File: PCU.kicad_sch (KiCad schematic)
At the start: 12 parts, among them J11 Screw_Terminal_01x01, U4 EPC2152, Y1 AMDLA4020S-220MT

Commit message: Final addings
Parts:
- removed J11: Screw_Terminal_01x01, TerminalBlock_Phoenix:TerminalBlock_Phoenix_MKDS-1,5-2-5.08_1x02_P5.08mm_Horizontal, symbol Connector:Screw_Terminal_01x01
- added J11: Screw_Terminal_01x04, TerminalBlock_Phoenix:TerminalBlock_Phoenix_MKDS-1,5-4-5.08_1x04_P5.08mm_Horizontal, symbol Connector:Screw_Terminal_01x04
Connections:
- net V_in_12V: now also J11.1 (Pin_1)
- net V_out: now also J11.2 (Pin_2)
- net at C8.1, U4.1 (Vdd12F): now also J11.3 (Pin_3)
- new net GND: J11.4 (Pin_4)
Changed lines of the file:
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@@
+	)
+	(junction
+		(at 149.86 52.07)
+		(diameter 0)
+		(color 0 0 0 0)
 	)
 	(junction
@@
 	(wire
 		(pts
+			(xy 59.69 45.72) (xy 66.04 45.72)
+		)
+		(stroke
+			(width 0)
+			(type default)
+		)
+	)
+	(wire
+		(pts
 			(xy 187.96 87.63) (xy 177.8 87.63)
 		)
@@
 	(wire
 		(pts
+			(xy 66.04 45.72) (xy 66.04 52.07)
+		)
+		(stroke
+			(width 0)
+			(type default)
+		)
+	)
+	(wire
+		(pts
 			(xy 153.67 68.58) (xy 153.67 72.39)
 		)
@@
 	(wire
 		(pts
+			(xy 54.61 30.48) (xy 59.69 30.48)
+		)
+		(stroke
+			(width 0)
+			(type default)
+		)
+	)
+	(wire
+		(pts
+			(xy 54.61 27.94) (xy 189.23 27.94)
+		)
+		(stroke
+			(width 0)
+			(type default)
+		)
+	)
+	(wire
+		(pts
 			(xy 147.32 87.63) (xy 167.64 87.63)
 		)
@@
 	(wire
 		(pts
-			(xy 147.32 52.07) (xy 153.67 52.07)
+			(xy 59.69 30.48) (xy 59.69 45.72)
+		)
+		(stroke
+			(width 0)
+			(type default)
+		)
+	)
+	(wire
+		(pts
+			(xy 147.32 52.07) (xy 149.86 52.07)
 		)
 		(stroke
@@
 	(wire
 		(pts
+			(xy 54.61 20.32) (xy 54.61 22.86)
+		)
+		(stroke
+			(width 0)
+			(type default)
+		)
+	)
+	(wire
+		(pts
 			(xy 167.64 73.66) (xy 167.64 59.69)
 		)
@@
 	(wire
 		(pts
+			(xy 68.58 20.32) (xy 54.61 20.32)
+		)
+		(stroke
+			(width 0)
+			(type default)
+		)
+	)
+	(wire
+		(pts
+			(xy 149.86 52.07) (xy 153.67 52.07)
+		)
+		(stroke
+			(width 0)
+			(type default)
+		)
+	)
+	(wire
+		(pts
 			(xy 81.28 64.77) (xy 86.36 64.77)
 		)
@@
 	(wire
 		(pts
-			(xy 63.5 87.63) (xy 66.04 87.63)
+			(xy 149.86 52.07) (xy 149.86 25.4)
+		)
+		(stroke
+			(width 0)
+			(type default)
+		)
+	)
+	(wire
+		(pts
+			(xy 52.07 87.63) (xy 66.04 87.63)
 		)
 		(stroke
@@
 	(wire
 		(pts
+			(xy 149.86 25.4) (xy 54.61 25.4)
+		)
+		(stroke
+			(width 0)
+			(type default)
+		)
+	)
+	(wire
+		(pts
 			(xy 187.96 60.96) (xy 187.96 72.39)
+		)
+		(stroke
+			(width 0)
+			(type default)
+		)
+	)
+	(wire
+		(pts
+			(xy 189.23 27.94) (xy 189.23 60.96)
 		)
 		(stroke
@@
 	(hierarchical_label "GROUND"
 		(shape input)
-		(at 63.5 87.63 180)
+		(at 52.07 87.63 180)
 		(effects
 			(font
@@
 			)
 			(justify right)
+		)
+	)
+	(symbol
+		(lib_id "power:GND")
+		(at 68.58 20.32 0)
+		(unit 1)
+		(exclude_from_sim no)
+		(in_bom yes)
+		(on_board yes)
+		(dnp no)
+		(fields_autoplaced yes)
+		(property "Reference" "#PWR033"
+			(at 68.58 26.67 0)
+			(effects
+				(font
+					(size 1.27 1.27)
+				)
+				(hide yes)
+			)
+		)
+		(property "Value" "GND"
+			(at 68.58 25.4 0)
+			(effects
+				(font
+					(size 1.27 1.27)
+				)
+			)
+		)
+		(property "Footprint" ""
+			(at 68.58 20.32 0)
+			(effects
+				(font
+					(size 1.27 1.27)
+				)
+				(hide yes)
+			)
+		)
+		(property "Datasheet" ""
+			(at 68.58 20.32 0)
+			(effects
+				(font
+					(size 1.27 1.27)
+				)
+				(hide yes)
+			)
+		)
+		(property "Description" "Power symbol creates a global label with name \"GND\" , ground"
+			(at 68.58 20.32 0)
+			(effects
+				(font
+					(size 1.27 1.27)
+				)
+				(hide yes)
+			)
+		)
+		(pin "1"
+		)
+		(instances
+			(project "PULSE_ENG"
+				(path "/2de881bb-2e2a-47f9-96ed-b3393fa36b98/32fac869-3c72-4ec8-a514-1800b5db5371"
+					(reference "#PWR033")
+					(unit 1)
+				)
+			)
 		)
 	)
@@
 	)
 	(symbol
-		(lib_id "Connector:Screw_Terminal_01x01")
-		(at 194.31 60.96 0)
-		(unit 1)
-		(exclude_from_sim no)
-		(in_bom yes)
-		(on_board yes)
-		(dnp no)
-		(fields_autoplaced yes)
-		(property "Reference" "J11"
-			(at 196.85 59.6899 0)
-			(effects
-				(font
-					(size 1.27 1.27)
-				)
-				(justify left)
-			)
-		)
-		(property "Value" "Screw_Terminal_01x01"
-			(at 196.85 62.2299 0)
-			(effects
-				(font
-					(size 1.27 1.27)
-				)
-				(justify left)
-			)
-		)
-		(property "Footprint" "TerminalBlock_Phoenix:TerminalBlock_Phoenix_MKDS-1,5-2-5.08_1x02_P5.08mm_Horizontal"
-			(at 194.31 60.96 0)
-			(effects
-				(font
-					(size 1.27 1.27)
-				)
-				(hide yes)
-			)
-		)
-		(property "Datasheet" "~"
-			(at 194.31 60.96 0)
-			(effects
-				(font
-					(size 1.27 1.27)
-				)
-				(hide yes)
-			)
-		)
-		(property "Description" "Generic screw terminal, single row, 01x01, script generated (kicad-library-utils/schlib/autogen/connector/)"
-			(at 194.31 60.96 0)
-			(effects
-				(font
-					(size 1.27 1.27)
-				)
-				(hide yes)
-			)
-		)
-		(pin "1"
-		)
-		(instances
-			(project "PULSE_ENG"
-				(path "/2de881bb-2e2a-47f9-96ed-b3393fa36b98/32fac869-3c72-4ec8-a514-1800b5db5371"
-					(reference "J11")
-					(unit 1)
-				)
-			)
-		)
-	)
-	(symbol
 		(lib_id "SamacSys_Parts:EPC2152")
 		(at 91.44 90.17 0)
@@
 					(unit 1)
 				)
+			)
+		)
+	)
+	(symbol
+		(lib_id "Connector:Screw_Terminal_01x04")
+		(at 49.53 27.94 180)
+		(unit 1)
+		(exclude_from_sim no)
+		(in_bom yes)
+		(on_board yes)
+		(dnp no)
+		(fields_autoplaced yes)
+		(property "Reference" "J11"
+			(at 49.53 16.51 0)
+			(effects
+				(font
+					(size 1.27 1.27)
+				)
+			)
+		)
+		(property "Value" "Screw_Terminal_01x04"
+			(at 49.53 19.05 0)
+			(effects
+				(font
+					(size 1.27 1.27)
+				)
+			)
+		)
+		(property "Footprint" "TerminalBlock_Phoenix:TerminalBlock_Phoenix_MKDS-1,5-4-5.08_1x04_P5.08mm_Horizontal"
+			(at 49.53 27.94 0)
+			(effects
+				(font
+					(size 1.27 1.27)
+				)
+				(hide yes)
+			)
+		)
+		(property "Datasheet" "~"
+			(at 49.53 27.94 0)
+			(effects
+				(font
+					(size 1.27 1.27)
+				)
+				(hide yes)
+			)
+		)
+		(property "Description" "Generic screw terminal, single row, 01x04, script generated (kicad-library-utils/schlib/autogen/connector/)"
+			(at 49.53 27.94 0)
+			(effects
+				(font
+					(size 1.27 1.27)
+				)
+				(hide yes)
+			)
+		)
+		(pin "1"
+		)
+		(pin "2"
+		)
+		(pin "3"
+		)
+		(pin "4"
+		)
+		(instances
+			(project "PULSE_ENG"
+				(path "/2de881bb-2e2a-47f9-96ed-b3393fa36b98/32fac869-3c72-4ec8-a514-1800b5db5371"
+					(reference "J11")
+					(unit 1)
+				)

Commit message: Modofications asked and BOM
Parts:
- J11: Mouser Part Number (none) -> 651-1701144; Mouser link (none) -> https://www.mouser.ch/ProductDetail/Phoenix-Contact/1701144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
- L2: footprint Inductor_THT:L_Axial_L7.0mm_D3.3mm_P10.16mm_Horizontal_Fastron_MICC -> Inductor_SMD:L_0603_1608Metric
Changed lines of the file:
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@@
+			)
+		)
+		(property "Mouser Part Number" "651-1701144"
+			(at 49.53 27.94 0)
+			(effects
+				(font
+					(size 1.27 1.27)
+				)
+				(hide yes)
+			)
+		)
+		(property "Mouser link" "https://www.mouser.ch/ProductDetail/Phoenix-Contact/1701144?qs=2WS7V4AoKFp2%2F3%2FlSacg6Q%3D%3D"
+			(at 49.53 27.94 0)
+			(effects
+				(font
+					(size 1.27 1.27)
+				)
+				(hide yes)
 			)
 		)
@@
 			)
 		)
-		(property "Footprint" "Inductor_THT:L_Axial_L7.0mm_D3.3mm_P10.16mm_Horizontal_Fastron_MICC"
+		(property "Footprint" "Inductor_SMD:L_0603_1608Metric"
 			(at 161.29 72.39 0)
 			(effects

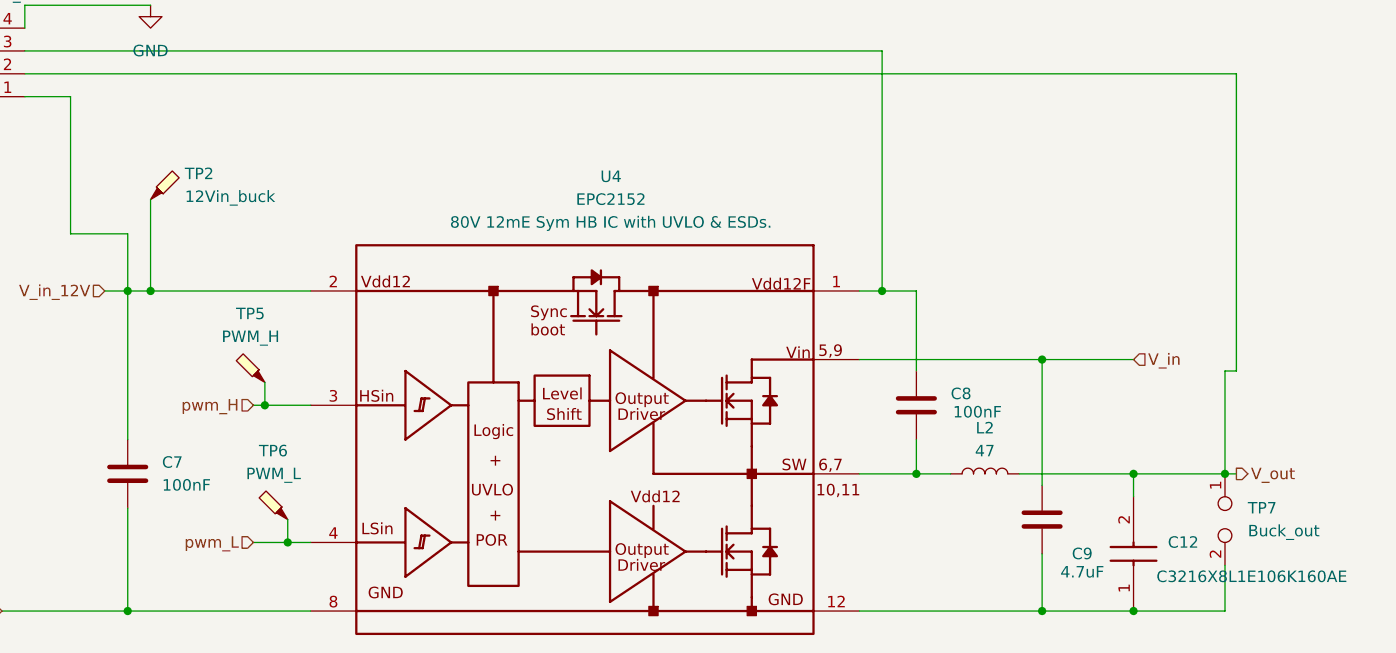
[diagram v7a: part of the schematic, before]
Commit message: changed mcu power suppl
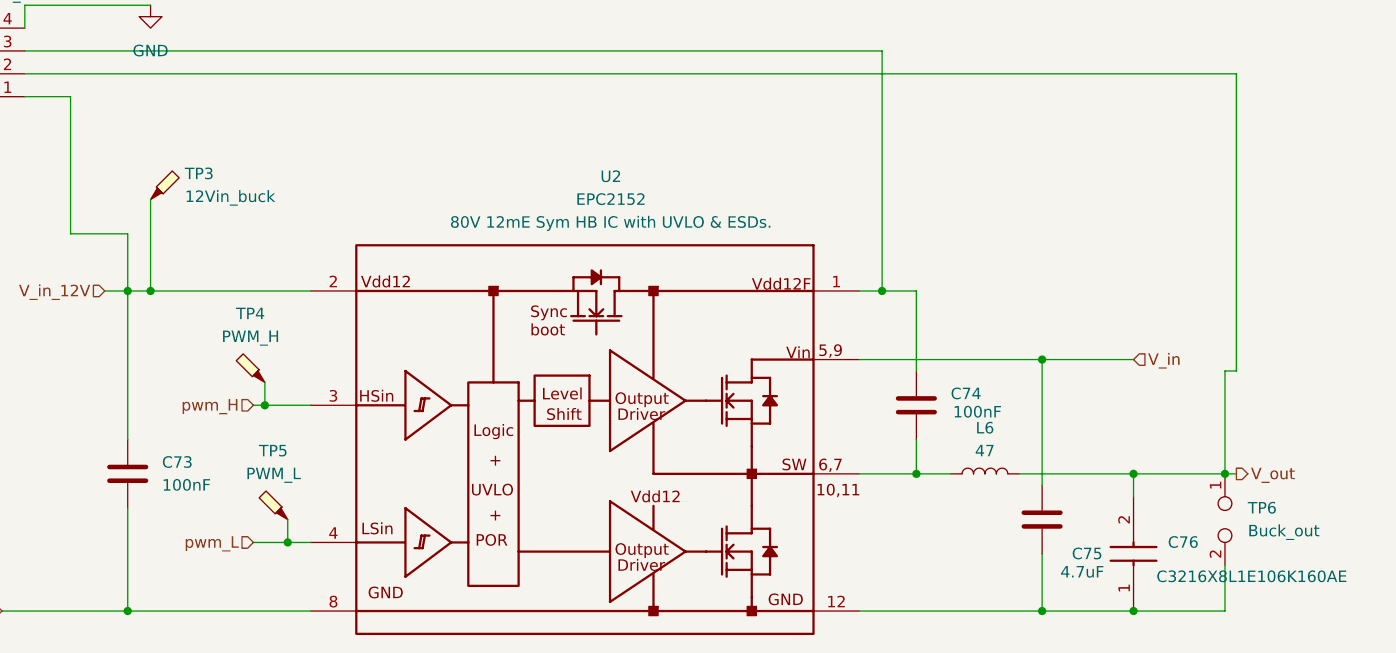
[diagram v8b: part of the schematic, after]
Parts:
- renumbered C7 to C73, C8 to C74, C9 to C75, C12 to C76, L2 to L6, TP2 to TP3, TP5 to TP4, TP6 to TP5, TP7 to TP6, U4 to U2
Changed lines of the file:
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@@
 		(dnp no)
 		(fields_autoplaced yes)
-		(property "Reference" "#PWR033"
+		(property "Reference" "#PWR048"
 			(at 68.58 26.67 0)
 			(effects
@@
 			(project "PULSE_ENG"
 				(path "/2de881bb-2e2a-47f9-96ed-b3393fa36b98/32fac869-3c72-4ec8-a514-1800b5db5371"
-					(reference "#PWR033")
+					(reference "#PWR048")
 					(unit 1)
 				)
@@
 		(dnp no)
 		(fields_autoplaced yes)
-		(property "Reference" "TP2"
+		(property "Reference" "TP3"
 			(at 72.39 39.0524 0)
 			(effects
@@
 			(project ""
 				(path "/2de881bb-2e2a-47f9-96ed-b3393fa36b98/32fac869-3c72-4ec8-a514-1800b5db5371"
-					(reference "TP2")
+					(reference "TP3")
 					(unit 1)
 				)
@@
 		(on_board yes)
 		(dnp no)
-		(property "Reference" "C12"
+		(property "Reference" "C76"
 			(at 181.61 80.0099 90)
 			(effects
@@
 			(project "PULSE_ENG"
 				(path "/2de881bb-2e2a-47f9-96ed-b3393fa36b98/32fac869-3c72-4ec8-a514-1800b5db5371"
-					(reference "C12")
+					(reference "C76")
 					(unit 1)
 				)
@@
 		(dnp no)
 		(fields_autoplaced yes)
-		(property "Reference" "TP6"
+		(property "Reference" "TP5"
 			(at 82.2325 69.85 90)
 			(effects
@@
 			(project "PULSE_ENG"
 				(path "/2de881bb-2e2a-47f9-96ed-b3393fa36b98/32fac869-3c72-4ec8-a514-1800b5db5371"
-					(reference "TP6")
+					(reference "TP5")
 					(unit 1)
 				)
@@
 		(on_board yes)
 		(dnp no)
-		(property "Reference" "C8"
+		(property "Reference" "C74"
 			(at 157.48 63.4999 0)
 			(effects
@@
 			(project "PULSE_ENG"
 				(path "/2de881bb-2e2a-47f9-96ed-b3393fa36b98/32fac869-3c72-4ec8-a514-1800b5db5371"
-					(reference "C8")
+					(reference "C74")
 					(unit 1)
 				)
@@
 		(dnp no)
 		(fields_autoplaced yes)
-		(property "Reference" "TP7"
+		(property "Reference" "TP6"
 			(at 190.5 76.1999 90)
 			(effects
@@
 			(project ""
 				(path "/2de881bb-2e2a-47f9-96ed-b3393fa36b98/32fac869-3c72-4ec8-a514-1800b5db5371"
-					(reference "TP7")
+					(reference "TP6")
 					(unit 1)
 				)
@@
 		(on_board yes)
 		(dnp no)
-		(property "Reference" "C9"
+		(property "Reference" "C75"
 			(at 170.942 81.28 0)
 			(effects
@@
 			(project "PULSE_ENG"
 				(path "/2de881bb-2e2a-47f9-96ed-b3393fa36b98/32fac869-3c72-4ec8-a514-1800b5db5371"
-					(reference "C9")
+					(reference "C75")
 					(unit 1)
 				)
@@
 		(dnp no)
 		(fields_autoplaced yes)
-		(property "Reference" "C7"
+		(property "Reference" "C73"
 			(at 69.85 71.1199 0)
 			(effects
@@
 			(project "PULSE_ENG"
 				(path "/2de881bb-2e2a-47f9-96ed-b3393fa36b98/32fac869-3c72-4ec8-a514-1800b5db5371"
-					(reference "C7")
+					(reference "C73")
 					(unit 1)
 				)
@@
 		(dnp no)
 		(fields_autoplaced yes)
-		(property "Reference" "U4"
+		(property "Reference" "U2"
 			(at 119.7361 39.37 0)
 			(effects
@@
 			(project "PULSE_ENG"
 				(path "/2de881bb-2e2a-47f9-96ed-b3393fa36b98/32fac869-3c72-4ec8-a514-1800b5db5371"
-					(reference "U4")
+					(reference "U2")
 					(unit 1)
 				)
@@
 		(dnp no)
 		(fields_autoplaced yes)
-		(property "Reference" "L2"
+		(property "Reference" "L6"
 			(at 161.29 67.31 90)
 			(effects
@@
 			(project "PULSE_ENG"
 				(path "/2de881bb-2e2a-47f9-96ed-b3393fa36b98/32fac869-3c72-4ec8-a514-1800b5db5371"
-					(reference "L2")
+					(reference "L6")
 					(unit 1)
 				)
@@
 		(dnp no)
 		(fields_autoplaced yes)
-		(property "Reference" "TP5"
+		(property "Reference" "TP4"
 			(at 79.6925 54.61 90)
 			(effects
@@
 			(project ""
 				(path "/2de881bb-2e2a-47f9-96ed-b3393fa36b98/32fac869-3c72-4ec8-a514-1800b5db5371"
-					(reference "TP5")
-					(unit 1)
-				)
+					(reference "TP4")
+					(unit 1)
+				)
